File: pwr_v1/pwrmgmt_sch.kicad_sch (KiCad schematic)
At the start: 11 parts, among them J1 Conn_01x02, U1 LM2576S-5, U2 LM2576S-12

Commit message: Schematic updated
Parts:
- renumbered J1 to BAT1
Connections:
- net GND renamed VN
- net VBAT renamed VP

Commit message: Schematic and layout updated
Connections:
- net VN renamed GND
- net VP renamed VBAT
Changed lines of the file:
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@@
+	(wire
+		(pts
+			(xy 107.95 95.25) (xy 107.95 99.06)
+		)
+		(stroke
+			(width 0)
+			(type default)
+		)
+	)
 	(wire
 		(pts
@@
 	(wire
 		(pts
+			(xy 105.41 57.15) (xy 105.41 60.96)
+		)
+		(stroke
+			(width 0)
+			(type default)
+		)
+	)
+	(wire
+		(pts
 			(xy 120.65 83.82) (xy 123.19 83.82)
 		)
@@
 		)
 	)
-	(label "VN"
+	(label "GND"
 		(at 59.69 64.77 0)
 		(fields_autoplaced yes)
@@
 		)
 	)
-	(label "VP"
+	(label "VBAT"
 		(at 87.63 78.74 0)
 		(fields_autoplaced yes)
@@
 		)
 	)
-	(label "VN"
-		(at 105.41 57.15 0)
+	(label "VBAT"
+		(at 59.69 55.88 0)
 		(fields_autoplaced yes)
 		(effects
@@
 		)
 	)
-	(label "VN"
-		(at 107.95 95.25 0)
+	(label "VBAT"
+		(at 85.09 40.64 0)
 		(fields_autoplaced yes)
 		(effects
@@
 		)
 	)
-	(label "VP"
-		(at 59.69 55.88 0)
+	(hierarchical_label "5V"
+		(shape input)
+		(at 140.97 40.64 0)
 		(fields_autoplaced yes)
 		(effects
@@
 				(size 1.27 1.27)
 			)
-			(justify left bottom)
-		)
-	)
-	(label "VP"
-		(at 85.09 40.64 0)
+			(justify left)
+		)
+	)
+	(hierarchical_label "12V"
+		(shape input)
+		(at 143.51 78.74 0)
 		(fields_autoplaced yes)
 		(effects
@@
 				(size 1.27 1.27)
 			)
-			(justify left bottom)
-		)
-	)
-	(hierarchical_label "5V"
-		(shape input)
-		(at 140.97 40.64 0)
-		(fields_autoplaced yes)
-		(effects
-			(font
-				(size 1.27 1.27)
-			)
-			(justify left)
-		)
-	)
-	(hierarchical_label "12V"
-		(shape input)
-		(at 143.51 78.74 0)
-		(fields_autoplaced yes)
-		(effects
-			(font
-				(size 1.27 1.27)
-			)
 			(justify left)
 		)
@@
 			)
 		)
-		(property "Value" "VP"
+		(property "Value" "VBAT"
 			(at 60.96 50.038 0)
 			(effects
@@
 	)
 	(symbol
+		(lib_id "power:GND")
+		(at 105.41 60.96 0)
+		(unit 1)
+		(exclude_from_sim no)
+		(in_bom yes)
+		(on_board yes)
+		(dnp no)
+		(property "Reference" "#PWR054"
+			(at 105.41 67.31 0)
+			(effects
+				(font
+					(size 1.27 1.27)
+				)
+				(hide yes)
+			)
+		)
+		(property "Value" "GND"
+			(at 109.22 62.738 0)
+			(effects
+				(font
+					(size 1.27 1.27)
+				)
+			)
+		)
+		(property "Footprint" ""
+			(at 105.41 60.96 0)
+			(effects
+				(font
+					(size 1.27 1.27)
+				)
+				(hide yes)
+			)
+		)
+		(property "Datasheet" ""
+			(at 105.41 60.96 0)
+			(effects
+				(font
+					(size 1.27 1.27)
+				)
+				(hide yes)
+			)
+		)
+		(property "Description" "Power symbol creates a global label with name \"GND\" , ground"
+			(at 105.41 60.96 0)
+			(effects
+				(font
+					(size 1.27 1.27)
+				)
+				(hide yes)
+			)
+		)
+		(pin "1"
+		)
+		(instances
+			(project "pwr_v1"
+				(path "/42eee4f9-ea65-4e89-8296-df9554a24009/ab92c88f-83ff-4167-83e9-28d0c7b08887"
+					(reference "#PWR054")
+					(unit 1)
+				)
+			)
+		)
+	)
+	(symbol
 		(lib_id "Device:D")
 		(at 123.19 90.17 270)
@@
 			)
 		)
-		(property "Value" "VN"
+		(property "Value" "GND"
 			(at 63.5 70.358 0)
 			(effects
@@
 					(unit 1)
 				)
+			)
+		)
+	)
+	(symbol
+		(lib_id "power:GND")
+		(at 107.95 99.06 0)
+		(unit 1)
+		(exclude_from_sim no)
+		(in_bom yes)
+		(on_board yes)
+		(dnp no)
+		(property "Reference" "#PWR055"
+			(at 107.95 105.41 0)
+			(effects
+				(font
+					(size 1.27 1.27)
+				)
+				(hide yes)
+			)
+		)
+		(property "Value" "GND"
+			(at 111.76 100.838 0)
+			(effects
+				(font
+					(size 1.27 1.27)
+				)
+			)
+		)
+		(property "Footprint" ""
+			(at 107.95 99.06 0)
+			(effects
+				(font
+					(size 1.27 1.27)
+				)
+				(hide yes)
+			)
+		)
+		(property "Datasheet" ""
+			(at 107.95 99.06 0)
+			(effects
+				(font
+					(size 1.27 1.27)
+				)
+				(hide yes)
+			)
+		)
+		(property "Description" "Power symbol creates a global label with name \"GND\" , ground"
+			(at 107.95 99.06 0)
+			(effects
+				(font
+					(size 1.27 1.27)
+				)
+				(hide yes)
+			)
+		)
+		(pin "1"
+		)
+		(instances
+			(project "pwr_v1"
+				(path "/42eee4f9-ea65-4e89-8296-df9554a24009/ab92c88f-83ff-4167-83e9-28d0c7b08887"
+					(reference "#PWR055")
+					(unit 1)
+				)

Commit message: Schematic updated
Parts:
- removed BAT1: Conn_01x02, TerminalBlock_4Ucon:TerminalBlock_4Ucon_1x02_P3.50mm_Horizontal, symbol Connector_Generic:Conn_01x02

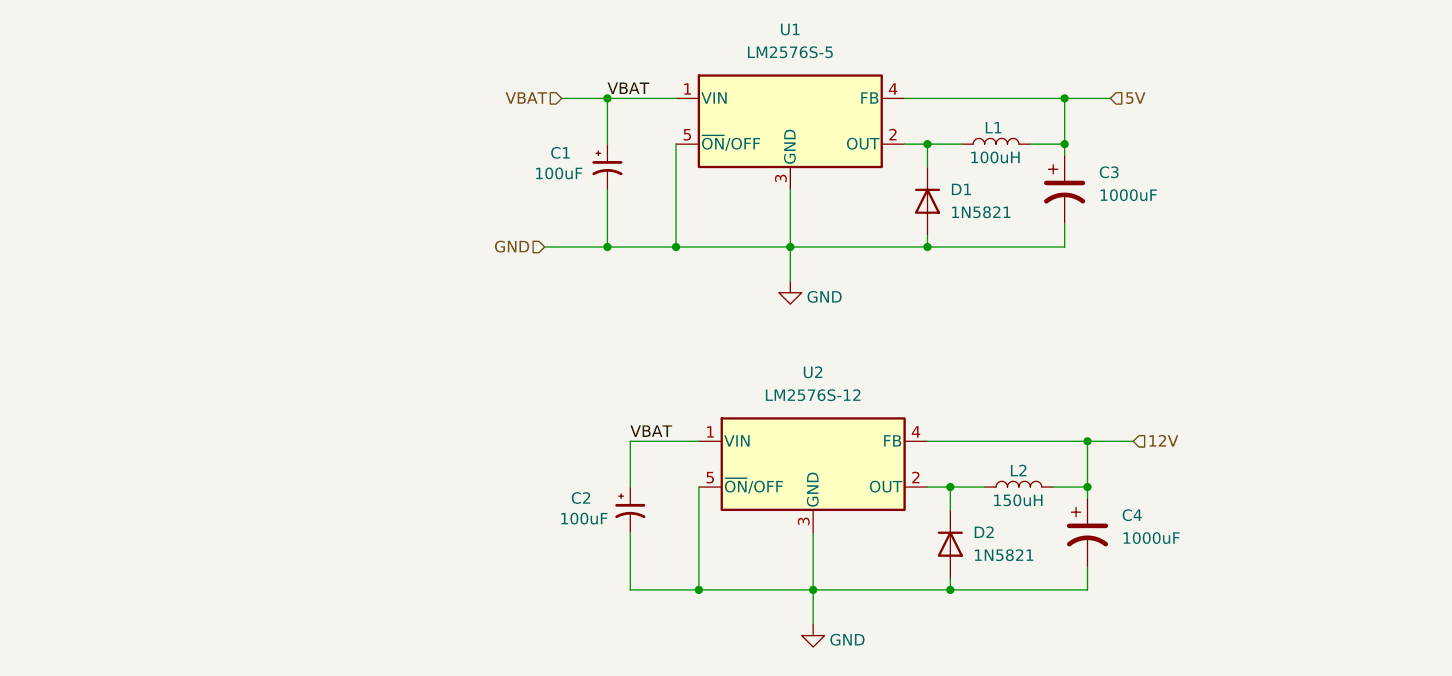
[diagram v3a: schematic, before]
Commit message: Schematic updated; Layout updated; STM PinMappings file added
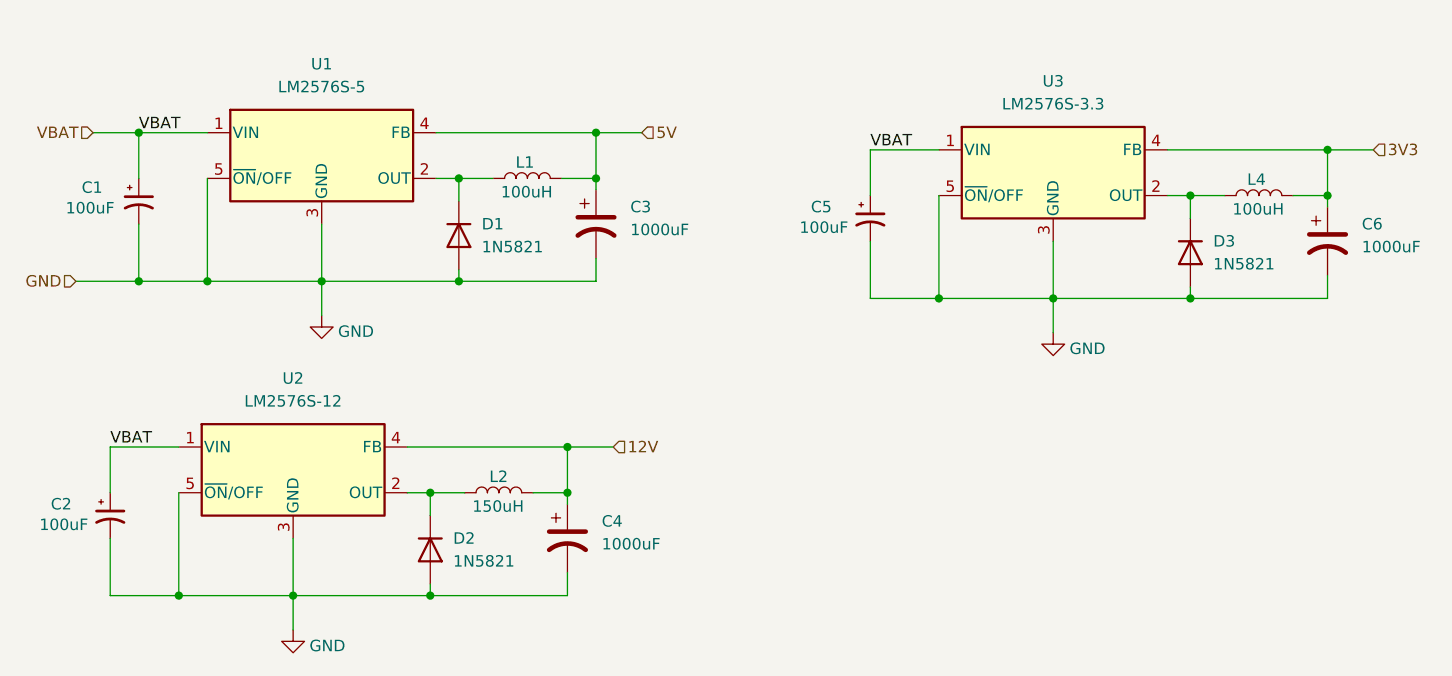
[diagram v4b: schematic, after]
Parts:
- added C5: 100uF, Capacitor_SMD:CP_Elec_8x10, symbol Device:C_Polarized_Small_US
- added C6: 1000uF, Capacitor_SMD:CP_Elec_10x10.5, symbol Device:C_Polarized_US
- added D3: 1N5821, Diode_THT:D_DO-201AD_P15.24mm_Horizontal, symbol Device:D
- added L4: 100uH, Inductor_SMD:L_Sunlord_MWSA1206S-101, symbol Device:L
- added U3: LM2576S-3.3, Package_TO_SOT_SMD:TO-263-5_TabPin3, symbol Regulator_Switching:LM2576S-3.3
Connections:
- net GND: now also C5.2, C6.2, D3.2 (A), U3.3 (GND), U3.5 (~{ON}/OFF)
- net VBAT: now also C5.1, U3.1 (VIN)
- new net: D3.1 (K), L4.1, U3.2 (OUT)
- new net 3V3: C6.1, L4.2, U3.4 (FB)
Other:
- moved on the sheet: C1, C2, C3, C4, D1, D2, L1, L2, U1, U2

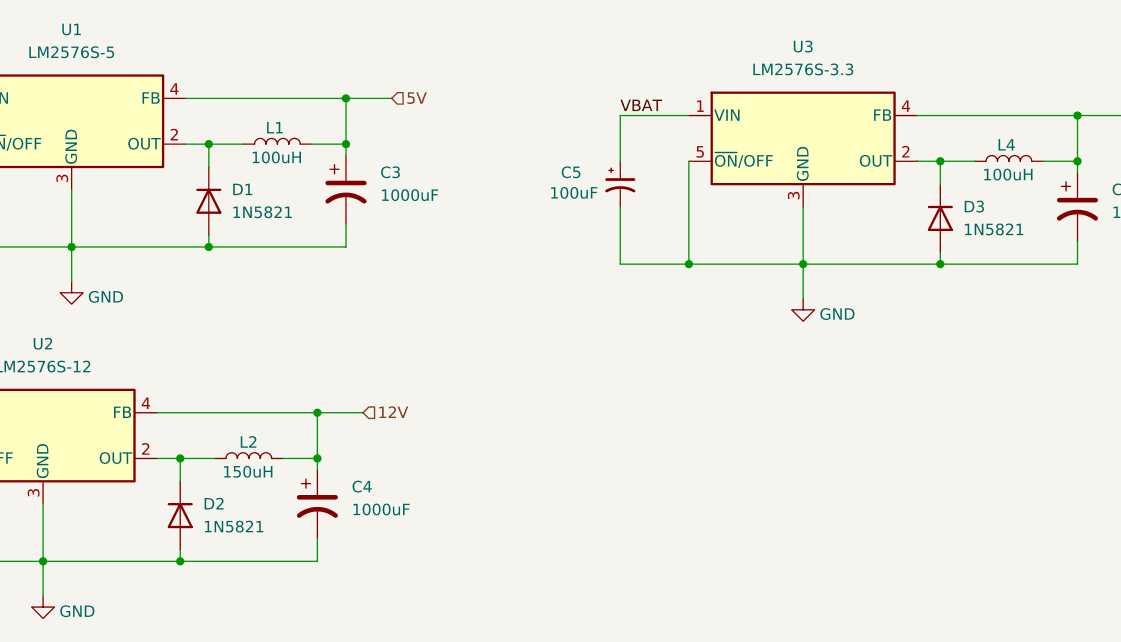
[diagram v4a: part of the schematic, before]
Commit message: Sch: DNP updated, JLC part numbers updated for all components; Lay: Fiducial placement, routing aligned.
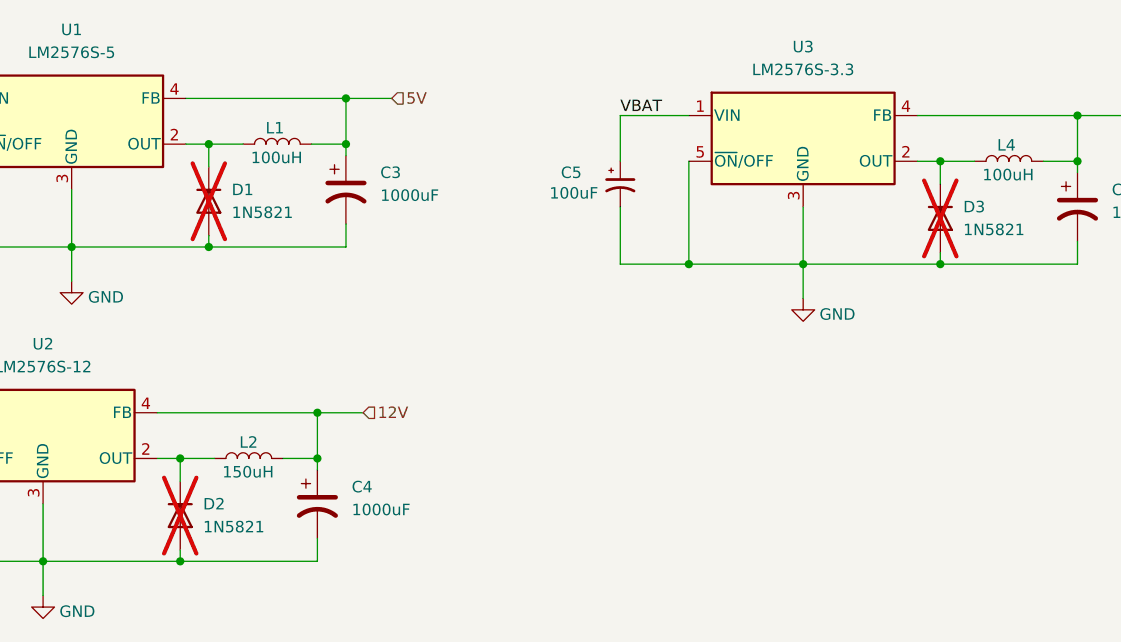
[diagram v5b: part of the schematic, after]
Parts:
- D1, D2, D3: now not fitted; now left out of the parts list
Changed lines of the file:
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@@
 		(unit 1)
 		(exclude_from_sim no)
-		(in_bom yes)
-		(on_board yes)
-		(dnp no)
+		(in_bom no)
+		(on_board yes)
+		(dnp yes)
 		(fields_autoplaced yes)
 		(property "Reference" "D2"
@@
 		(unit 1)
 		(exclude_from_sim no)
-		(in_bom yes)
-		(on_board yes)
-		(dnp no)
+		(in_bom no)
+		(on_board yes)
+		(dnp yes)
 		(fields_autoplaced yes)
 		(property "Reference" "D3"
@@
 		(unit 1)
 		(exclude_from_sim no)
-		(in_bom yes)
-		(on_board yes)
-		(dnp no)
+		(in_bom no)
+		(on_board yes)
+		(dnp yes)
 		(fields_autoplaced yes)
 		(property "Reference" "D1"

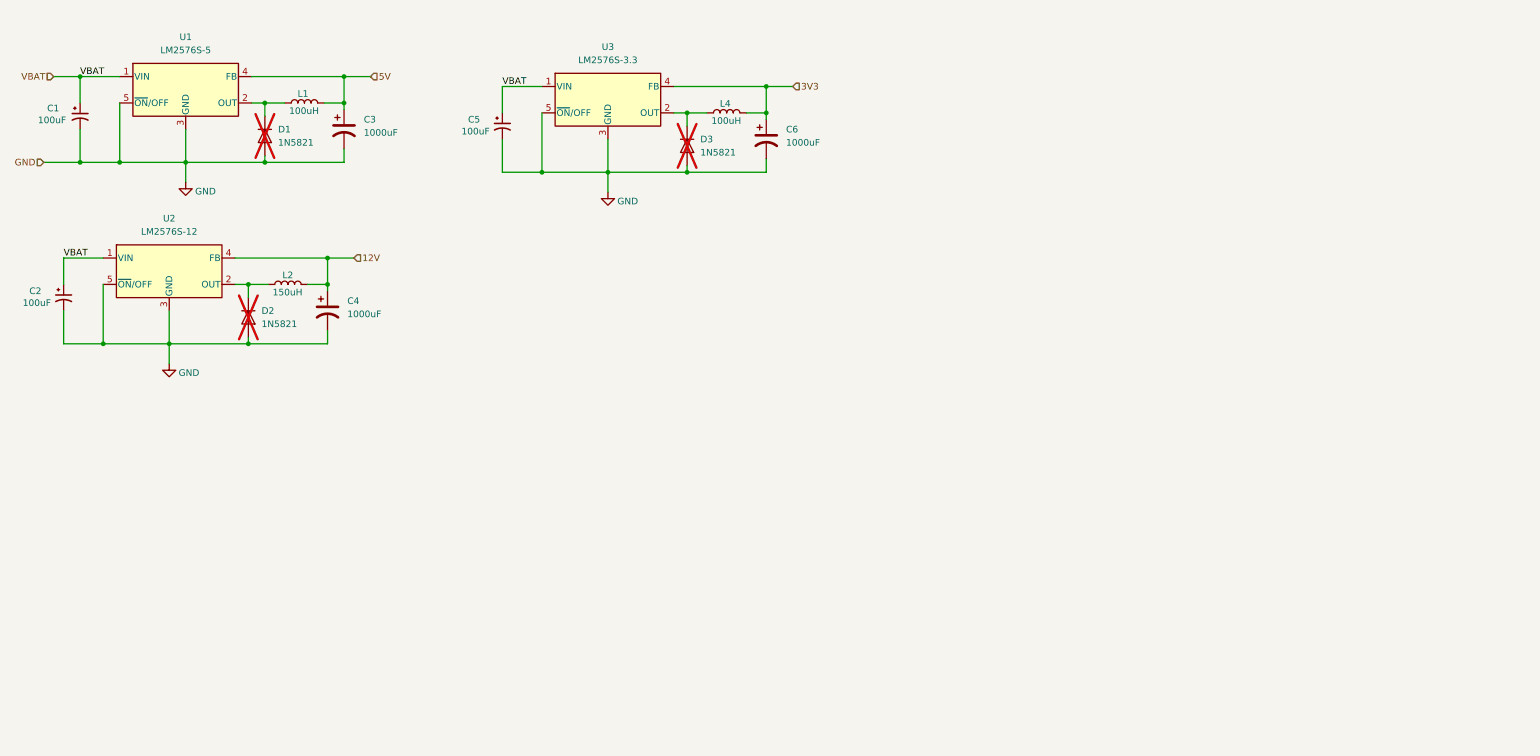
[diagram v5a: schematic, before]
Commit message: File structure enhanced.
Added uniform titleblocks and 3D renders for easier view, file cleanups.
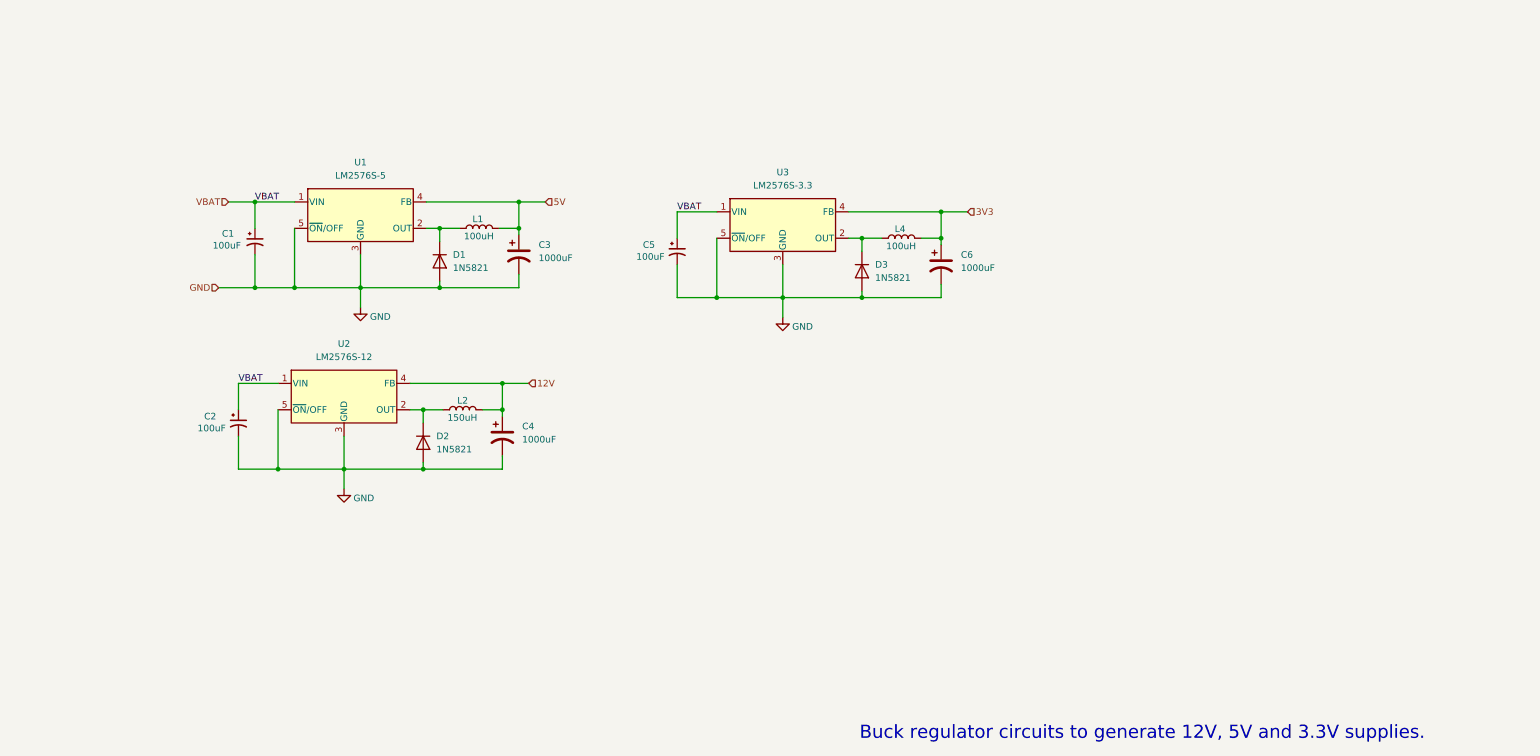
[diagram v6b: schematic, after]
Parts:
- D1, D2, D3: now fitted
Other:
- note added: "Buck regulator circuits to generate 12V, 5V and 3.3V supplies."
- title: (none) -> Power board
- moved on the sheet: C1, C2, C3, C4, C5, C6, L1, L2, L4, U1, U2, U3
